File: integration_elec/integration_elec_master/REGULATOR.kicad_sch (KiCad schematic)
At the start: 24 parts, among them U4 TPS54335ADDAR

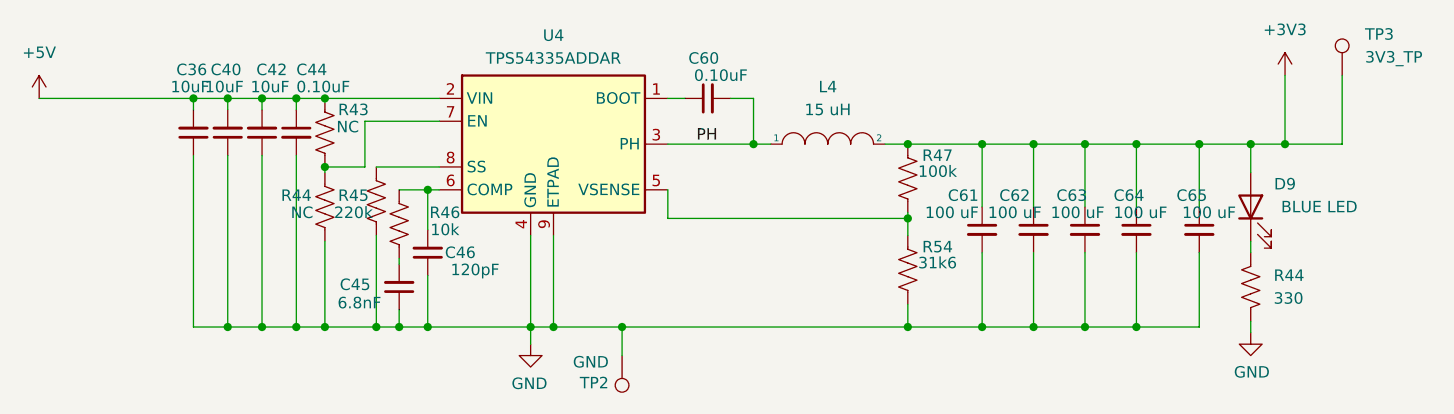
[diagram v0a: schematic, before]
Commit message: Added footprint, symbol, 3D model for joystick. Added schematic for Joystick and comments
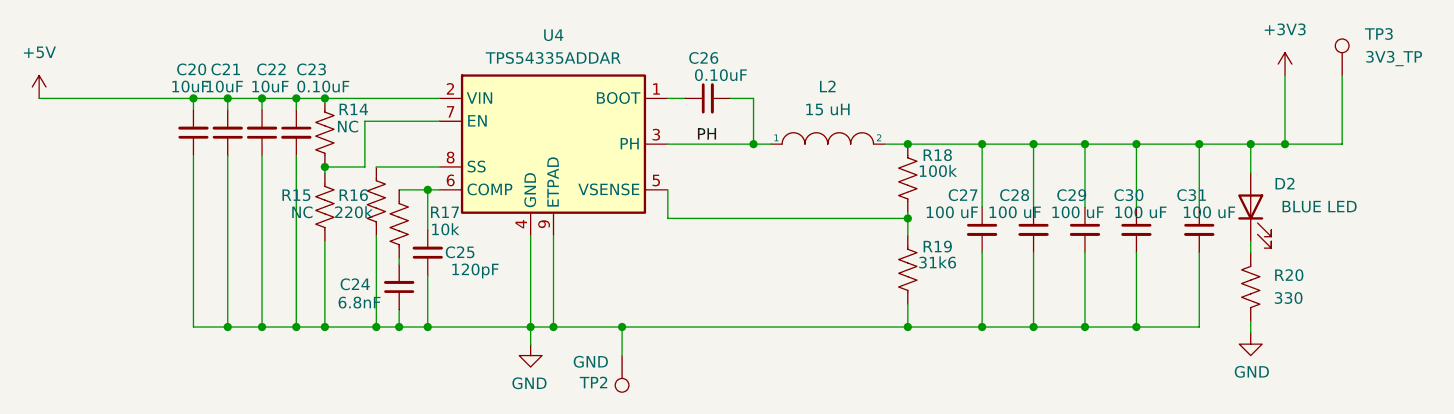
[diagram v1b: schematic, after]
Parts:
- renumbered C36 to C20, C40 to C21, C42 to C22, C44 to C23, C45 to C24, C46 to C25, C60 to C26, C61 to C27, C62 to C28, C63 to C29, C64 to C30, C65 to C31, D9 to D2, L4 to L2, R43 to R14, R44 to R15, R45 to R16, R46 to R17, R47 to R18, R54 to R19, R44 to R20
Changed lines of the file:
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@@
 		(on_board yes)
 		(dnp no)
-		(property "Reference" "R47"
+		(property "Reference" "R18"
 			(at 165.862 77.47 0)
 			(effects
@@
 			(project "integration_elec_master"
 				(path "/7d904e0d-c2b1-4329-81a9-fc34d181a4fe/b6550ae5-c9f3-4780-b288-b1ff08ddf5fe"
-					(reference "R47")
+					(reference "R18")
 					(unit 1)
 				)
@@
 		(on_board yes)
 		(dnp no)
-		(property "Reference" "C44"
+		(property "Reference" "C23"
 			(at 94.615 67.945 0)
 			(effects
@@
 			(project "integration_elec_master"
 				(path "/7d904e0d-c2b1-4329-81a9-fc34d181a4fe/b6550ae5-c9f3-4780-b288-b1ff08ddf5fe"
-					(reference "C44")
+					(reference "C23")
 					(unit 1)
 				)
@@
 		(on_board yes)
 		(dnp no)
-		(property "Reference" "D9"
+		(property "Reference" "D2"
 			(at 204.47 80.645 90)
 			(effects
@@
 			(project "integration_elec_master"
 				(path "/7d904e0d-c2b1-4329-81a9-fc34d181a4fe/b6550ae5-c9f3-4780-b288-b1ff08ddf5fe"
-					(reference "D9")
+					(reference "D2")
 					(unit 1)
 				)
@@
 		(dnp no)
 		(fields_autoplaced yes)
-		(property "Reference" "#PWR019"
+		(property "Reference" "#PWR029"
 			(at 66.04 74.93 0)
 			(effects
@@
 			(project ""
 				(path "/7d904e0d-c2b1-4329-81a9-fc34d181a4fe/b6550ae5-c9f3-4780-b288-b1ff08ddf5fe"
-					(reference "#PWR019")
+					(reference "#PWR029")
 					(unit 1)
 				)
@@
 		(on_board yes)
 		(dnp no)
-		(property "Reference" "R45"
+		(property "Reference" "R16"
 			(at 100.965 81.915 0)
 			(effects
@@
 			(project "integration_elec_master"
 				(path "/7d904e0d-c2b1-4329-81a9-fc34d181a4fe/b6550ae5-c9f3-4780-b288-b1ff08ddf5fe"
-					(reference "R45")
+					(reference "R16")
 					(unit 1)
 				)
@@
 		(on_board yes)
 		(dnp no)
-		(property "Reference" "C36"
+		(property "Reference" "C20"
 			(at 81.28 67.945 0)
 			(effects
@@
 			(project "integration_elec_master"
 				(path "/7d904e0d-c2b1-4329-81a9-fc34d181a4fe/b6550ae5-c9f3-4780-b288-b1ff08ddf5fe"
-					(reference "C36")
+					(reference "C20")
 					(unit 1)
 				)
@@
 		(dnp no)
 		(fields_autoplaced yes)
-		(property "Reference" "#PWR020"
+		(property "Reference" "#PWR032"
 			(at 204.47 72.39 0)
 			(effects
@@
 			(project ""
 				(path "/7d904e0d-c2b1-4329-81a9-fc34d181a4fe/b6550ae5-c9f3-4780-b288-b1ff08ddf5fe"
-					(reference "#PWR020")
+					(reference "#PWR032")
 					(unit 1)
 				)
@@
 		(on_board yes)
 		(dnp no)
-		(property "Reference" "C63"
+		(property "Reference" "C29"
 			(at 179.07 81.915 0)
 			(effects
@@
 			(project "integration_elec_master"
 				(path "/7d904e0d-c2b1-4329-81a9-fc34d181a4fe/b6550ae5-c9f3-4780-b288-b1ff08ddf5fe"
-					(reference "C63")
+					(reference "C29")
 					(unit 1)
 				)
@@
 		(on_board yes)
 		(dnp no)
-		(property "Reference" "R54"
+		(property "Reference" "R19"
 			(at 165.862 87.63 0)
 			(effects
@@
 			(project "integration_elec_master"
 				(path "/7d904e0d-c2b1-4329-81a9-fc34d181a4fe/b6550ae5-c9f3-4780-b288-b1ff08ddf5fe"
-					(reference "R54")
+					(reference "R19")
 					(unit 1)
 				)
@@
 		(on_board yes)
 		(dnp no)
-		(property "Reference" "C62"
+		(property "Reference" "C28"
 			(at 172.72 81.915 0)
 			(effects
@@
 			(project "integration_elec_master"
 				(path "/7d904e0d-c2b1-4329-81a9-fc34d181a4fe/b6550ae5-c9f3-4780-b288-b1ff08ddf5fe"
-					(reference "C62")
+					(reference "C28")
 					(unit 1)
 				)
@@
 		(on_board yes)
 		(dnp no)
-		(property "Reference" "C42"
+		(property "Reference" "C22"
 			(at 90.17 67.945 0)
 			(effects
@@
 			(project "integration_elec_master"
 				(path "/7d904e0d-c2b1-4329-81a9-fc34d181a4fe/b6550ae5-c9f3-4780-b288-b1ff08ddf5fe"
-					(reference "C42")
+					(reference "C22")
 					(unit 1)
 				)
@@
 		(on_board yes)
 		(dnp no)
-		(property "Reference" "C40"
+		(property "Reference" "C21"
 			(at 85.09 67.945 0)
 			(effects
@@
 			(project "integration_elec_master"
 				(path "/7d904e0d-c2b1-4329-81a9-fc34d181a4fe/b6550ae5-c9f3-4780-b288-b1ff08ddf5fe"
-					(reference "C40")
+					(reference "C21")
 					(unit 1)
 				)
@@
 		(on_board yes)
 		(dnp no)
-		(property "Reference" "R44"
+		(property "Reference" "R15"
 			(at 94.615 81.915 0)
 			(effects
@@
 			(project "integration_elec_master"
 				(path "/7d904e0d-c2b1-4329-81a9-fc34d181a4fe/b6550ae5-c9f3-4780-b288-b1ff08ddf5fe"
-					(reference "R44")
+					(reference "R15")
 					(unit 1)
 				)
@@
 		(on_board yes)
 		(dnp no)
-		(property "Reference" "C64"
+		(property "Reference" "C30"
 			(at 185.42 81.915 0)
 			(effects
@@
 			(project "integration_elec_master"
 				(path "/7d904e0d-c2b1-4329-81a9-fc34d181a4fe/b6550ae5-c9f3-4780-b288-b1ff08ddf5fe"
-					(reference "C64")
+					(reference "C30")
 					(unit 1)
 				)
@@
 		(on_board yes)
 		(dnp no)
-		(property "Reference" "C65"
+		(property "Reference" "C31"
 			(at 192.405 81.915 0)
 			(effects
@@
 			(project "integration_elec_master"
 				(path "/7d904e0d-c2b1-4329-81a9-fc34d181a4fe/b6550ae5-c9f3-4780-b288-b1ff08ddf5fe"
-					(reference "C65")
+					(reference "C31")
 					(unit 1)
 				)
@@
 		(on_board yes)
 		(dnp no)
-		(property "Reference" "C45"
+		(property "Reference" "C24"
 			(at 99.441 91.821 0)
 			(effects
@@
 			(project "integration_elec_master"
 				(path "/7d904e0d-c2b1-4329-81a9-fc34d181a4fe/b6550ae5-c9f3-4780-b288-b1ff08ddf5fe"
-					(reference "C45")
+					(reference "C24")
 					(unit 1)
 				)
@@
 		(dnp no)
 		(fields_autoplaced yes)
-		(property "Reference" "L4"
+		(property "Reference" "L2"
 			(at 153.67 69.85 0)
 			(effects
@@
 			(project "integration_elec_master"
 				(path "/7d904e0d-c2b1-4329-81a9-fc34d181a4fe/b6550ae5-c9f3-4780-b288-b1ff08ddf5fe"
-					(reference "L4")
+					(reference "L2")
 					(unit 1)
 				)
@@
 		(on_board yes)
 		(dnp no)
-		(property "Reference" "C46"
+		(property "Reference" "C25"
 			(at 111.125 88.265 0)
 			(effects
@@
 			(project "integration_elec_master"
 				(path "/7d904e0d-c2b1-4329-81a9-fc34d181a4fe/b6550ae5-c9f3-4780-b288-b1ff08ddf5fe"
-					(reference "C46")
+					(reference "C25")
 					(unit 1)
 				)
@@
 		(on_board yes)
 		(dnp no)
-		(property "Reference" "R43"
+		(property "Reference" "R14"
 			(at 100.965 72.39 0)
 			(effects
@@
 			(project "integration_elec_master"
 				(path "/7d904e0d-c2b1-4329-81a9-fc34d181a4fe/b6550ae5-c9f3-4780-b288-b1ff08ddf5fe"
-					(reference "R43")
+					(reference "R14")
 					(unit 1)
 				)
@@
 		(on_board yes)
 		(dnp no)
-		(property "Reference" "#PWR065"
+		(property "Reference" "#PWR030"
 			(at 120.65 104.775 0)
 			(effects
@@
 			(project "integration_elec_master"
 				(path "/7d904e0d-c2b1-4329-81a9-fc34d181a4fe/b6550ae5-c9f3-4780-b288-b1ff08ddf5fe"
-					(reference "#PWR065")
+					(reference "#PWR030")
 					(unit 1)
 				)
@@
 		(on_board yes)
 		(dnp no)
-		(property "Reference" "R44"
+		(property "Reference" "R20"
 			(at 203.2 90.805 0)
 			(effects
@@
 			(project "integration_elec_master"
 				(path "/7d904e0d-c2b1-4329-81a9-fc34d181a4fe/b6550ae5-c9f3-4780-b288-b1ff08ddf5fe"
-					(reference "R44")
+					(reference "R20")
 					(unit 1)
 				)
@@
 		(on_board yes)
 		(dnp no)
-		(property "Reference" "C61"
+		(property "Reference" "C27"
 			(at 167.005 81.915 0)
 			(effects
@@
 			(project "integration_elec_master"
 				(path "/7d904e0d-c2b1-4329-81a9-fc34d181a4fe/b6550ae5-c9f3-4780-b288-b1ff08ddf5fe"
-					(reference "C61")
+					(reference "C27")
 					(unit 1)
 				)
@@
 		(on_board yes)
 		(dnp no)
-		(property "Reference" "R46"
+		(property "Reference" "R17"
 			(at 111.125 83.82 0)
 			(effects
@@
 			(project "integration_elec_master"
 				(path "/7d904e0d-c2b1-4329-81a9-fc34d181a4fe/b6550ae5-c9f3-4780-b288-b1ff08ddf5fe"
-					(reference "R46")
+					(reference "R17")
 					(unit 1)
 				)
@@
 		(on_board yes)
 		(dnp no)
-		(property "Reference" "#PWR075"
+		(property "Reference" "#PWR031"
 			(at 200.66 103.505 0)
 			(effects
@@
 			(project "integration_elec_master"
 				(path "/7d904e0d-c2b1-4329-81a9-fc34d181a4fe/b6550ae5-c9f3-4780-b288-b1ff08ddf5fe"
-					(reference "#PWR075")
+					(reference "#PWR031")
 					(unit 1)
 				)
@@
 		(on_board yes)
 		(dnp no)
-		(property "Reference" "C60"
+		(property "Reference" "C26"
 			(at 141.605 66.675 90)
 			(effects
@@
 			(project "integration_elec_master"
 				(path "/7d904e0d-c2b1-4329-81a9-fc34d181a4fe/b6550ae5-c9f3-4780-b288-b1ff08ddf5fe"
-					(reference "C60")
-					(unit 1)
-				)
+					(reference "C26")
+					(unit 1)
+				)

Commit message: Added plein de footprint
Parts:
- L2: footprint Inductors:IND_BOURNS_SRR1280 -> JOYSTICK:IND_BOURNS_SRR1280
- TP3: footprint (none) -> TestPoint:TestPoint_Plated_Hole_D2.0mm
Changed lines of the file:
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@@
 			)
 		)
-		(property "Footprint" ""
+		(property "Footprint" "TestPoint:TestPoint_Plated_Hole_D2.0mm"
 			(at 215.9 68.58 0)
 			(effects
@@
 			)
 		)
-		(property "Footprint" "Inductors:IND_BOURNS_SRR1280"
+		(property "Footprint" "JOYSTICK:IND_BOURNS_SRR1280"
 			(at 153.67 76.2 0)
 			(effects

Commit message: KAH - Fini schematic attente de review + correction BUS
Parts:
- renumbered R14 to R16, R15 to R17, R16 to R18, R17 to R19, R18 to R20, R19 to R21, R20 to R22
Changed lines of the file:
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@@
 		(on_board yes)
 		(dnp no)
-		(property "Reference" "R18"
+		(property "Reference" "R20"
 			(at 165.862 77.47 0)
 			(effects
@@
 			(project "integration_elec_master"
 				(path "/7d904e0d-c2b1-4329-81a9-fc34d181a4fe/b6550ae5-c9f3-4780-b288-b1ff08ddf5fe"
-					(reference "R18")
+					(reference "R20")
 					(unit 1)
 				)
@@
 		(on_board yes)
 		(dnp no)
-		(property "Reference" "R16"
+		(property "Reference" "R18"
 			(at 100.965 81.915 0)
 			(effects
@@
 			(project "integration_elec_master"
 				(path "/7d904e0d-c2b1-4329-81a9-fc34d181a4fe/b6550ae5-c9f3-4780-b288-b1ff08ddf5fe"
-					(reference "R16")
+					(reference "R18")
 					(unit 1)
 				)
@@
 		(on_board yes)
 		(dnp no)
-		(property "Reference" "R19"
+		(property "Reference" "R21"
 			(at 165.862 87.63 0)
 			(effects
@@
 			(project "integration_elec_master"
 				(path "/7d904e0d-c2b1-4329-81a9-fc34d181a4fe/b6550ae5-c9f3-4780-b288-b1ff08ddf5fe"
-					(reference "R19")
+					(reference "R21")
 					(unit 1)
 				)
@@
 		(on_board yes)
 		(dnp no)
-		(property "Reference" "R15"
+		(property "Reference" "R17"
 			(at 94.615 81.915 0)
 			(effects
@@
 			(project "integration_elec_master"
 				(path "/7d904e0d-c2b1-4329-81a9-fc34d181a4fe/b6550ae5-c9f3-4780-b288-b1ff08ddf5fe"
-					(reference "R15")
+					(reference "R17")
 					(unit 1)
 				)
@@
 		(on_board yes)
 		(dnp no)
-		(property "Reference" "R14"
+		(property "Reference" "R16"
 			(at 100.965 72.39 0)
 			(effects
@@
 			(project "integration_elec_master"
 				(path "/7d904e0d-c2b1-4329-81a9-fc34d181a4fe/b6550ae5-c9f3-4780-b288-b1ff08ddf5fe"
-					(reference "R14")
+					(reference "R16")
 					(unit 1)
 				)
@@
 		(on_board yes)
 		(dnp no)
-		(property "Reference" "R20"
+		(property "Reference" "R22"
 			(at 203.2 90.805 0)
 			(effects
@@
 			(project "integration_elec_master"
 				(path "/7d904e0d-c2b1-4329-81a9-fc34d181a4fe/b6550ae5-c9f3-4780-b288-b1ff08ddf5fe"
-					(reference "R20")
+					(reference "R22")
 					(unit 1)
 				)
@@
 		(on_board yes)
 		(dnp no)
-		(property "Reference" "R17"
+		(property "Reference" "R19"
 			(at 111.125 83.82 0)
 			(effects
@@
 			(project "integration_elec_master"
 				(path "/7d904e0d-c2b1-4329-81a9-fc34d181a4fe/b6550ae5-c9f3-4780-b288-b1ff08ddf5fe"
-					(reference "R17")
-					(unit 1)
-				)
+					(reference "R19")
+					(unit 1)
+				)

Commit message: KAH - added the part # for some pieces. MISSING R NC and USB-C conn
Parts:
- TP2, TP3: now left out of the parts list
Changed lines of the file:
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@@
 		(unit 1)
 		(exclude_from_sim no)
-		(in_bom yes)
+		(in_bom no)
 		(on_board yes)
 		(dnp no)
@@
 		(unit 1)
 		(exclude_from_sim no)
-		(in_bom yes)
-		(on_board yes)
-		(dnp no)
+		(in_bom no)
+		(on_board yes)
+		(dnp no)
